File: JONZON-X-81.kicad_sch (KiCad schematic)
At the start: 30 parts, among them SW1 SW_DIP_x03, U1 AY-3-8910, U2 74HCT74, U3 74HCT08, U4 74HCT11, U5 74HCT02

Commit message: added rev 1.3 to revision history.
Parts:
- U2, U3, U4, U5: footprint Package_DIP:DIP-14_W10.16mm_LongPads -> Package_DIP:DIP-14_W7.62mm_Socket_LongPads
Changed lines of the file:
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@@
 		(title "JONZON-X-81")
 		(date "2025-08-01")
-		(rev "1.2")
+		(rev "1.3")
 	)
 	(text "Address Decoding with DIP Switch Options \nfor PSG select addresses of A4,5 and 6 \nto allow up to 3 PSG's for up to 9 channel sound"
@@
 			)
 		)
-		(property "Footprint" "Package_DIP:DIP-14_W10.16mm_LongPads"
+		(property "Footprint" "Package_DIP:DIP-14_W7.62mm_Socket_LongPads"
 			(at 34.29 135.89 0)
 			(effects
@@
 			)
 		)
-		(property "Footprint" "Package_DIP:DIP-14_W10.16mm_LongPads"
+		(property "Footprint" "Package_DIP:DIP-14_W7.62mm_Socket_LongPads"
 			(at 265.43 90.17 0)
 			(effects
@@
 			)
 		)
-		(property "Footprint" "Package_DIP:DIP-14_W10.16mm_LongPads"
+		(property "Footprint" "Package_DIP:DIP-14_W7.62mm_Socket_LongPads"
 			(at 228.6 57.15 0)
 			(effects
@@
 			)
 		)
-		(property "Footprint" "Package_DIP:DIP-14_W10.16mm_LongPads"
+		(property "Footprint" "Package_DIP:DIP-14_W7.62mm_Socket_LongPads"
 			(at 260.35 134.62 0)
 			(effects
@@
 			)
 		)
-		(property "Footprint" "Package_DIP:DIP-14_W10.16mm_LongPads"
+		(property "Footprint" "Package_DIP:DIP-14_W7.62mm_Socket_LongPads"
 			(at 153.67 59.69 0)
 			(effects
@@
 			)
 		)
-		(property "Footprint" "Package_DIP:DIP-14_W10.16mm_LongPads"
+		(property "Footprint" "Package_DIP:DIP-14_W7.62mm_Socket_LongPads"
 			(at 190.5 96.52 0)
 			(effects
@@
 			)
 		)
-		(property "Footprint" "Package_DIP:DIP-14_W10.16mm_LongPads"
+		(property "Footprint" "Package_DIP:DIP-14_W7.62mm_Socket_LongPads"
 			(at 34.29 116.84 0)
 			(effects
@@
 			)
 		)
-		(property "Footprint" "Package_DIP:DIP-14_W10.16mm_LongPads"
+		(property "Footprint" "Package_DIP:DIP-14_W7.62mm_Socket_LongPads"
 			(at 146.05 83.82 0)
 			(effects
@@
 			)
 		)
-		(property "Footprint" "Package_DIP:DIP-14_W10.16mm_LongPads"
+		(property "Footprint" "Package_DIP:DIP-14_W7.62mm_Socket_LongPads"
 			(at 247.65 134.62 0)
 			(effects
@@
 			)
 		)
-		(property "Footprint" "Package_DIP:DIP-14_W10.16mm_LongPads"
+		(property "Footprint" "Package_DIP:DIP-14_W7.62mm_Socket_LongPads"
 			(at 234.95 134.62 0)
 			(effects
@@
 			)
 		)
-		(property "Footprint" "Package_DIP:DIP-14_W10.16mm_LongPads"
+		(property "Footprint" "Package_DIP:DIP-14_W7.62mm_Socket_LongPads"
 			(at 262.89 38.1 0)
 			(effects
@@
 			)
 		)
-		(property "Footprint" "Package_DIP:DIP-14_W10.16mm_LongPads"
+		(property "Footprint" "Package_DIP:DIP-14_W7.62mm_Socket_LongPads"
 			(at 254 59.69 0)
 			(effects
@@
 			)
 		)
-		(property "Footprint" "Package_DIP:DIP-14_W10.16mm_LongPads"
+		(property "Footprint" "Package_DIP:DIP-14_W7.62mm_Socket_LongPads"
 			(at 204.47 40.64 0)
 			(effects
@@
 			)
 		)
-		(property "Footprint" "Package_DIP:DIP-14_W10.16mm_LongPads"
+		(property "Footprint" "Package_DIP:DIP-14_W7.62mm_Socket_LongPads"
 			(at 273.05 134.62 0)
 			(effects
@@
 			)
 		)
-		(property "Footprint" "Package_DIP:DIP-14_W10.16mm_LongPads"
+		(property "Footprint" "Package_DIP:DIP-14_W7.62mm_Socket_LongPads"
 			(at 143.51 29.21 0)
 			(effects
@@
 			)
 		)
-		(property "Footprint" "Package_DIP:DIP-14_W10.16mm_LongPads"
+		(property "Footprint" "Package_DIP:DIP-14_W7.62mm_Socket_LongPads"
 			(at 173.99 38.1 0)
 			(effects
@@
 			)
 		)
-		(property "Footprint" "Package_DIP:DIP-14_W10.16mm_LongPads"
+		(property "Footprint" "Package_DIP:DIP-14_W7.62mm_Socket_LongPads"
 			(at 146.05 99.06 0)
 			(effects

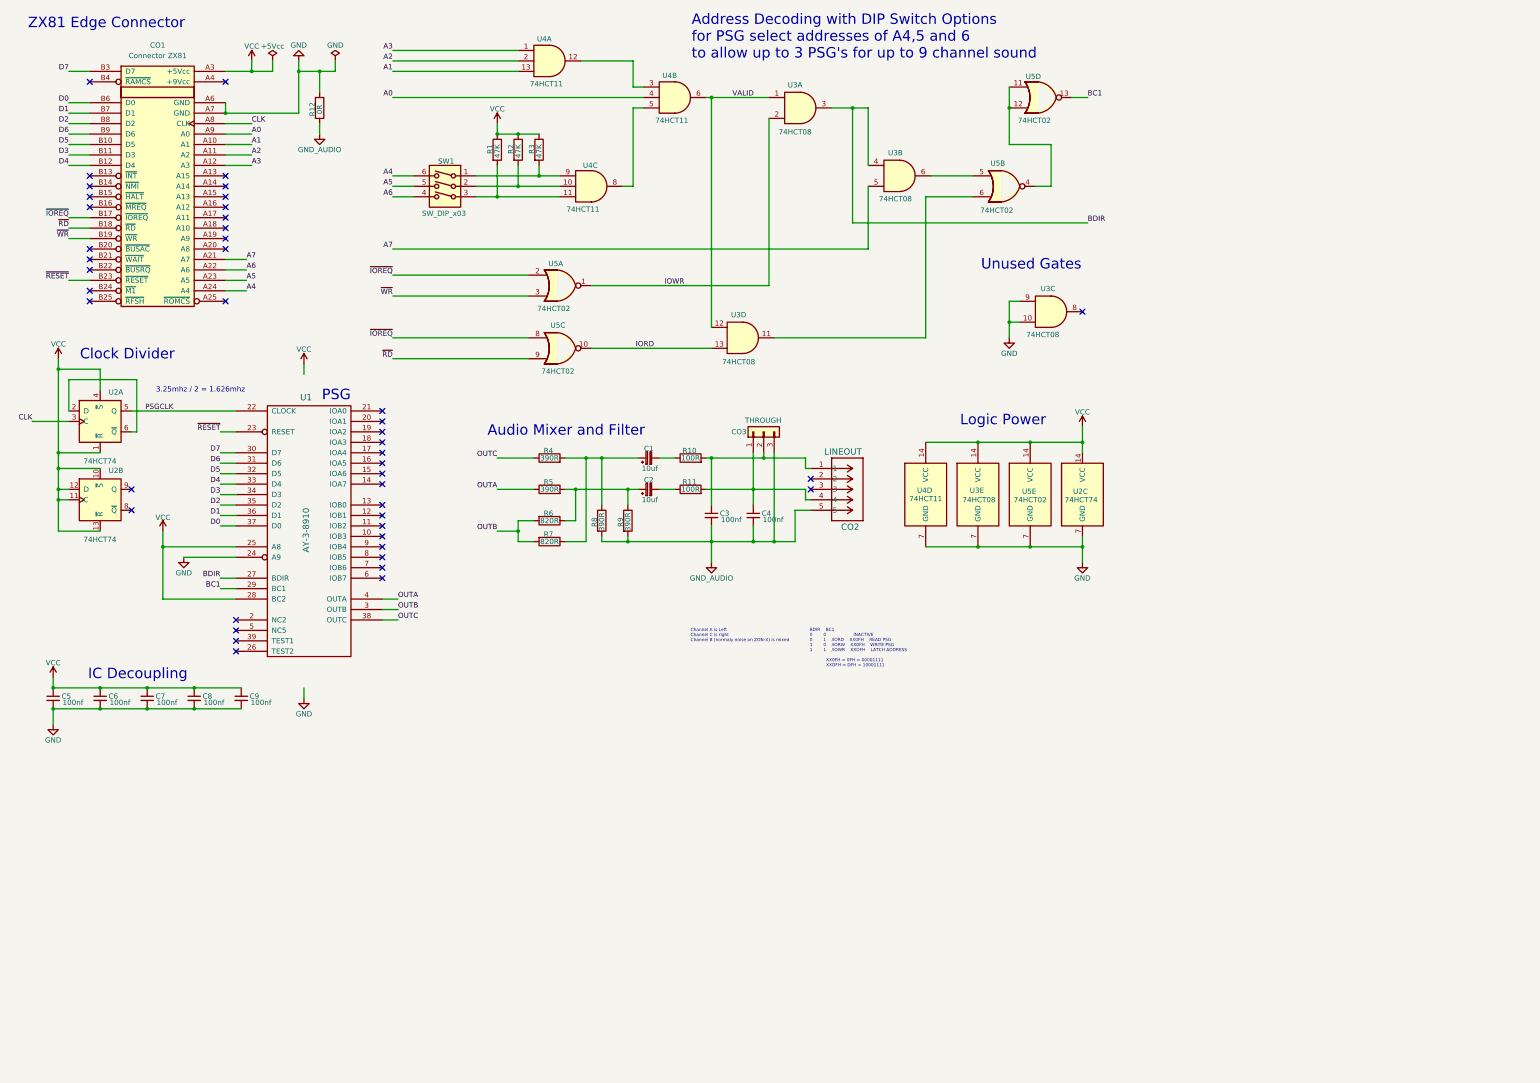
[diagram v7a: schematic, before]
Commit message: Added AY-3-8912 as an optional PSG to the Schematic. Created new v1.4 PDF.
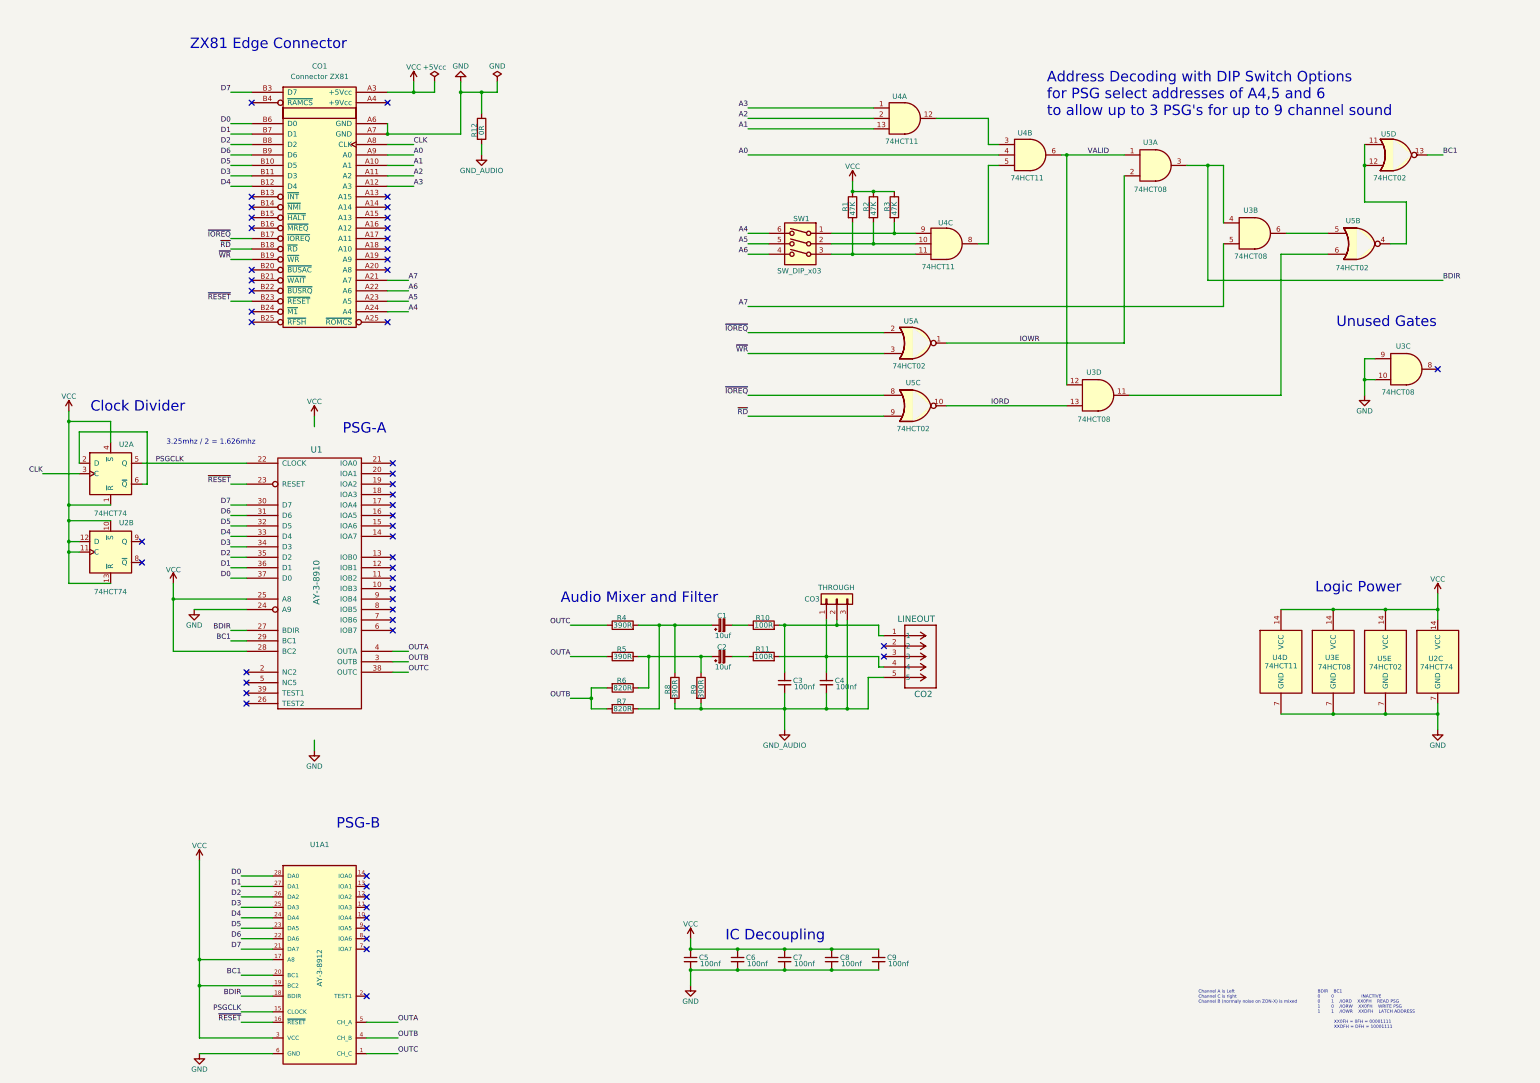
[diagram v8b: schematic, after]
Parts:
- added U1A1: AY-3-8912, symbol AY-3-8912:AY-3-8912
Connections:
- net BC1: now also U1A1.20 (BC1)
- net BDIR: now also U1A1.18 (BDIR)
- net D0: now also U1A1.28 (DA0)
- net D1: now also U1A1.27 (DA1)
- net D2: now also U1A1.26 (DA2)
- net D3: now also U1A1.25 (DA3)
- net D4: now also U1A1.24 (DA4)
- net D5: now also U1A1.23 (DA5)
- net D6: now also U1A1.22 (DA6)
- net D7: now also U1A1.21 (DA7)
- net GND: now also U1A1.6 (GND)
- net OUTA: now also U1A1.5 (CH_A)
- net OUTB: now also U1A1.4 (CH_B)
- net OUTC: now also U1A1.1 (CH_C)
- net PSGCLK: now also U1A1.15 (CLOCK)
- net VCC: now also U1A1.17 (A8), U1A1.19 (BC2), U1A1.3 (VCC)
- net ~{RESET}: now also U1A1.16 (~{RESET})
- no-connect marks 45 -> 54
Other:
- note added: "PSG-A"
- note added: "PSG-B"
- note removed: "PSG"
- moved on the sheet: C1, C2, C3, C4, C5, C6, C7, C8, C9, CO1, CO2, CO3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
